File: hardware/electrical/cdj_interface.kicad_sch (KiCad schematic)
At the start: 10 parts

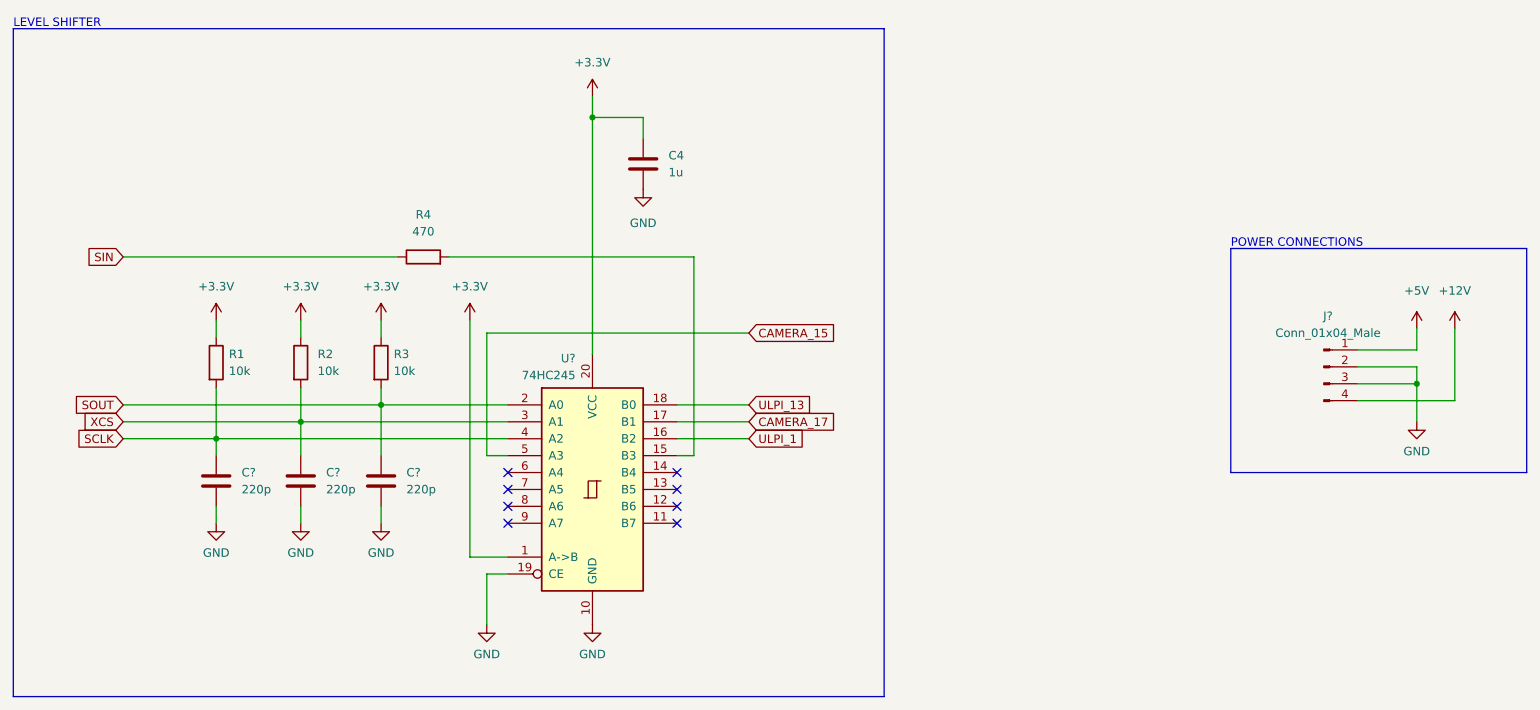
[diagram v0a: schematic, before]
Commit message: Schematic rev. 2 Add second microcontroller to handle encoder, buttons and LEDs Remove external pull-up resistors Simplify LED driver circuits Remove debouncing capacitors Rename SPI connections with standard names Use SPI1 rather than SPI2 Isolate GNDD and GLED
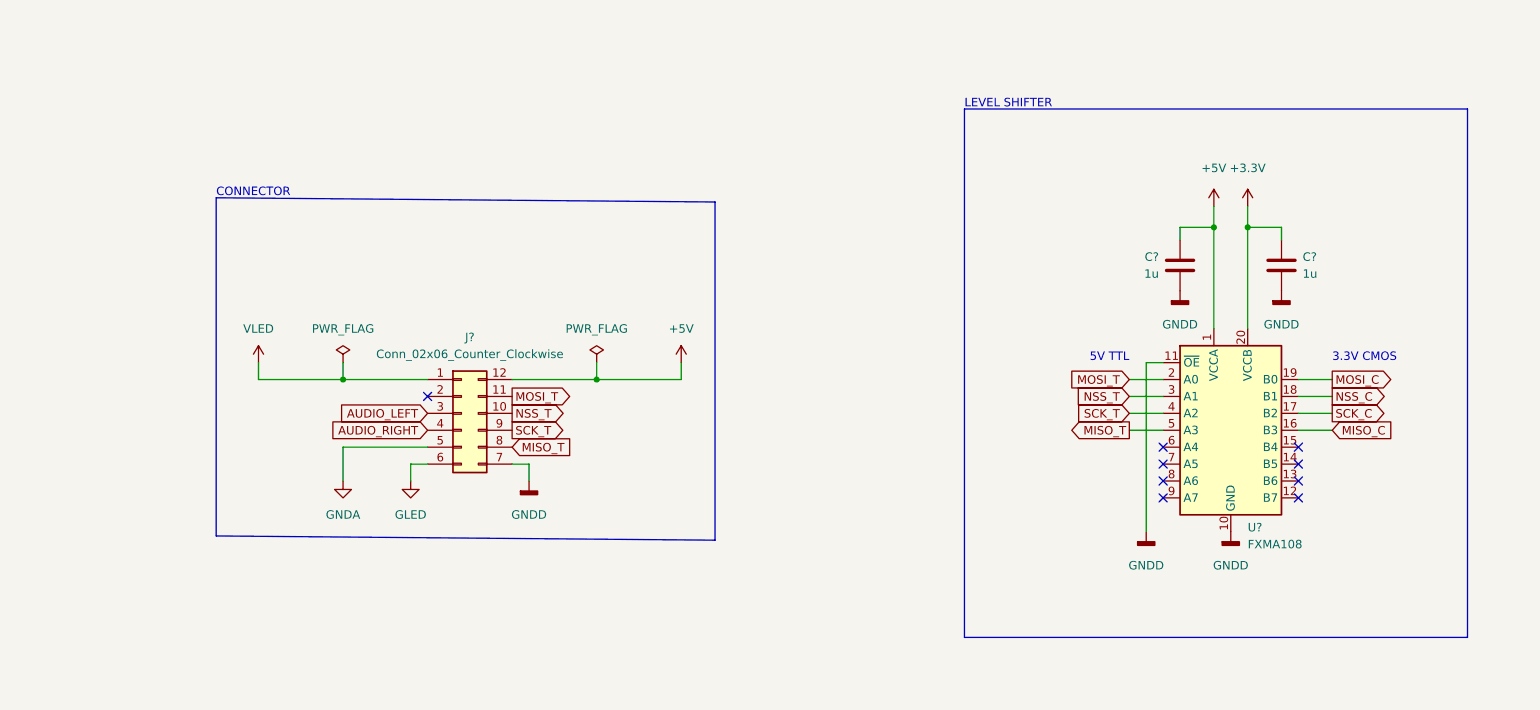
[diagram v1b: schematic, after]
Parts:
- removed C4: 1u, symbol Device:C
- removed C? (x3): 220p, symbol Device:C
- removed J?: Conn_01x04_Male, symbol Connector:Conn_01x04_Male
- removed R1, R2, R3: 10k, symbol Device:R
- removed R4: 470, symbol Device:R
- removed U?: 74HC245, symbol 74xx:74HC245
- added C? (x2): 1u, symbol Device:C
- added J?: Conn_02x06_Counter_Clockwise, symbol Connector_Generic:Conn_02x06_Counter_Clockwise
- added U?: FXMA108, Package_DFN_QFN:WQFN-20-1EP_2.5x4.5mm_P0.5mm_EP1x2.9mm, symbol Logic_LevelTranslator:FXMA108
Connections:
- net +3.3V: now also C?.1, U?.20 (VCCB)
- net +5V: now also C?.1, J?.12 (Pin_12), U?.1 (VCCA)
- new net AUDIO_LEFT: J?.3 (Pin_3)
- new net AUDIO_RIGHT: J?.4 (Pin_4)
- new net GLED: J?.6 (Pin_6)
- new net GNDA: J?.5 (Pin_5)
- new net GNDD: C?.2, C?.2, J?.7 (Pin_7), U?.10 (GND), U?.11 (~{OE})
- new net MISO_C: U?.16 (B3)
- new net MISO_T: J?.8 (Pin_8), U?.5 (A3)
- new net MOSI_C: U?.19 (B0)
- new net MOSI_T: J?.11 (Pin_11), U?.2 (A0)
- new net NSS_C: U?.18 (B1)
- new net NSS_T: J?.10 (Pin_10), U?.3 (A1)
- new net SCK_C: U?.17 (B2)
- new net SCK_T: J?.9 (Pin_9), U?.4 (A2)
- new net VLED: J?.1 (Pin_1)
- no-connect marks 8 -> 9
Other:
- note added: "3.3V CMOS"
- note added: "5V TTL"
- note added: "CONNECTOR"
- note removed: "POWER CONNECTIONS"
- company: (none) -> © ANDREI ANATSKA, FRANK PLOWMAN 2022
